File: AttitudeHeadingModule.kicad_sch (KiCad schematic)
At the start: 8 parts, among them J2 Conn_01x04, U2 BMI088, U3 MMC5983MA

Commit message: Change pressure connector from JST-GH-BM04B to JST-GH-SM04B
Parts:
- J2: footprint Connector_JST:JST_GH_BM04B-GHS-TBT_1x04-1MP_P1.25mm_Vertical -> Connector_JST:JST_GH_SM04B-GHS-TB_1x04-1MP_P1.25mm_Horizontal; Listing https://www.digikey.com/en/products/detail/jst-sales-america-inc/BM04B-GHS-TBT-LF-SN-N/807802 -> https://www.digikey.com/en/products/detail/jst-sales-america-inc/SM04B-GHS-TB/807788
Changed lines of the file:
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@@
 			)
 		)
-		(property "Footprint" "Connector_JST:JST_GH_BM04B-GHS-TBT_1x04-1MP_P1.25mm_Vertical"
+		(property "Footprint" "Connector_JST:JST_GH_SM04B-GHS-TB_1x04-1MP_P1.25mm_Horizontal"
 			(at 231.394 74.93 0)
 			(effects
@@
 			)
 		)
-		(property "Listing" "https://www.digikey.com/en/products/detail/jst-sales-america-inc/BM04B-GHS-TBT-LF-SN-N/807802"
+		(property "Listing" "https://www.digikey.com/en/products/detail/jst-sales-america-inc/SM04B-GHS-TB/807788"
 			(at 228.6 86.36 0)
 			(effects

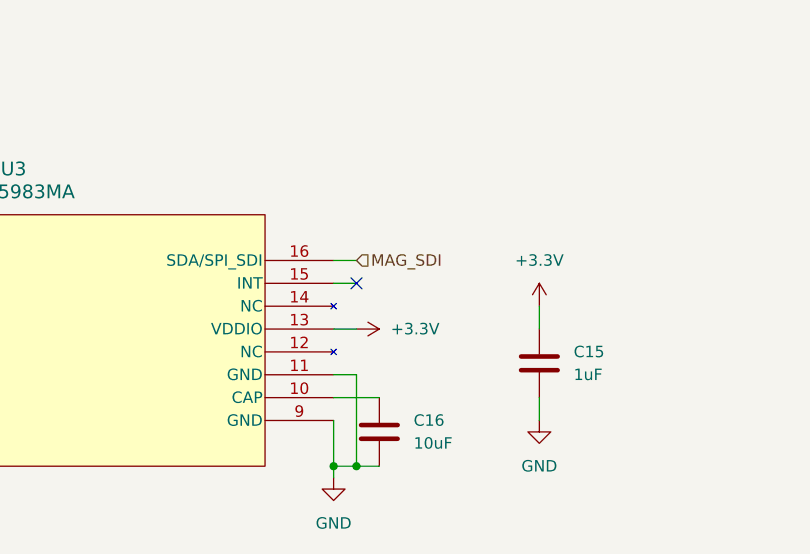
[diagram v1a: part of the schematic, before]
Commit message: Connect MCU interrupt pins to sensors
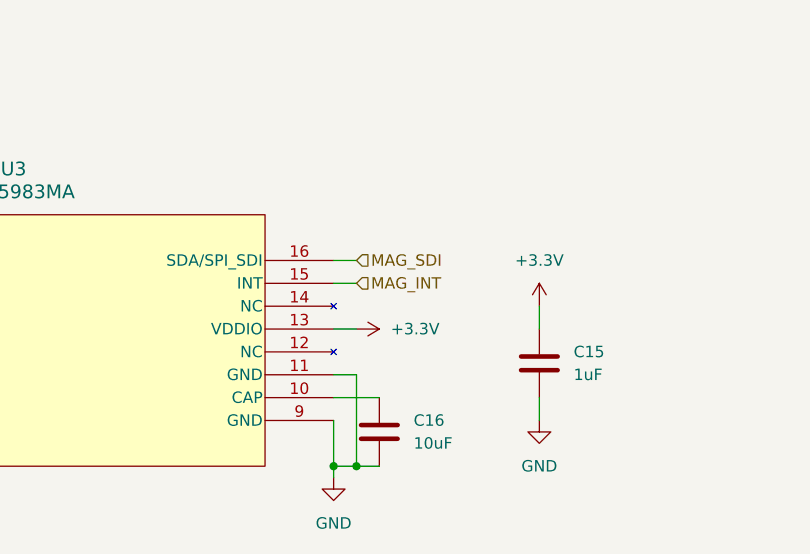
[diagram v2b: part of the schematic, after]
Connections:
- net MAG_INT: now reaches U3.15 (INT)
- no-connect marks 1 -> 0
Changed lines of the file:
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@@
 	(title_block
 		(title "Attitude and Heading Module")
-		(date "2025-12-21")
-		(rev "A")
+		(date "2026-01-28")
+		(rev "B")
 		(company "CU Boulder Senior Design Team 29 - Xu Lab")
 	)
@@
 		(color 0 0 0 0)
 	)
-	(no_connect
-		(at 119.38 110.49)
-	)
 	(wire
 		(pts
@@
 		)
 	)
+	(hierarchical_label "MAG_INT"
+		(shape input)
+		(at 119.38 110.49 0)
+		(effects
+			(font
+				(size 1.27 1.27)
+			)
+			(justify left)
+		)
+	)
